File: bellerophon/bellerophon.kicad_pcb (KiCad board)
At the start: 2 copper layers, 55 x 98 mm, 27 parts, among them IC1 L7805ACV, IC2 Adafruit_MPL3115A2, Q1 IRLB8721PBF, Q2 IRLB8721PBF, U1 Adafruit_ICM20948, U2 Teensy4.0, U3 Adafruit SPI Flash SD Card

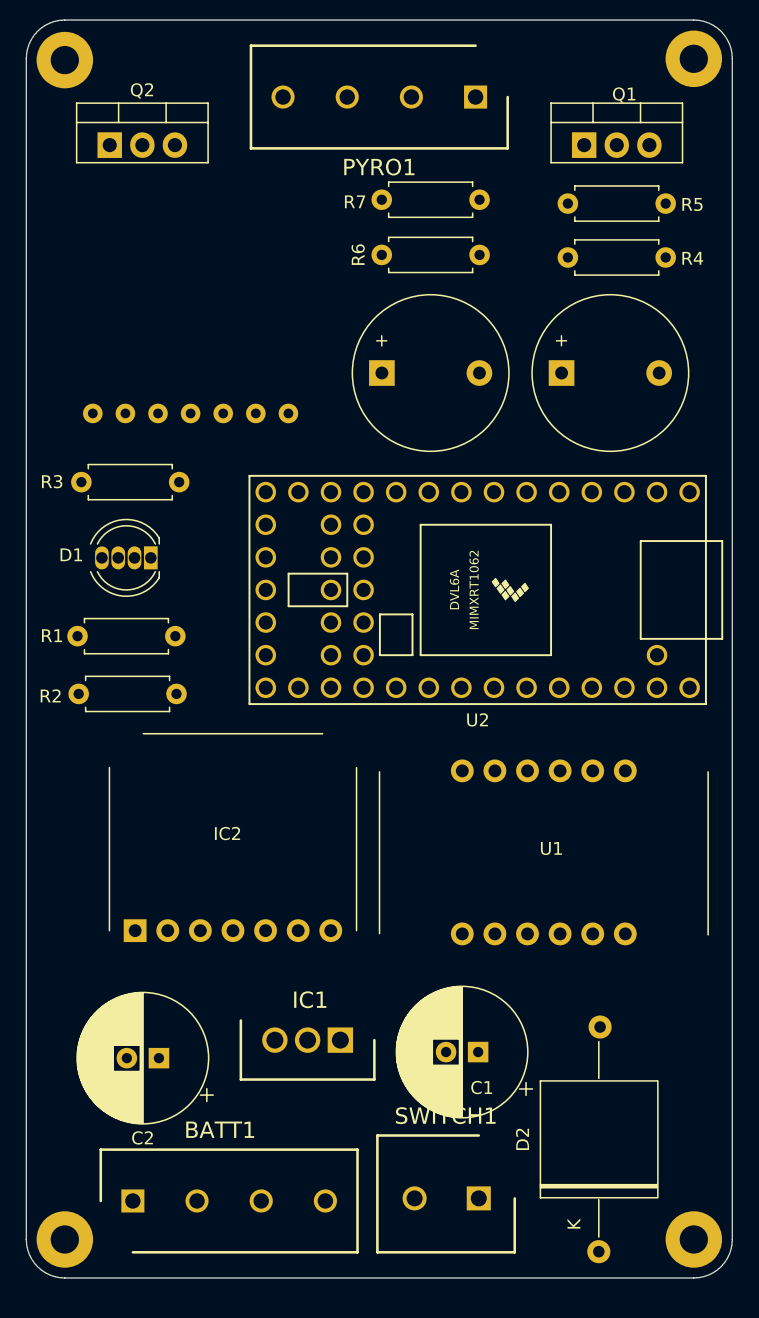
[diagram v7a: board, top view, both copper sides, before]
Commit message: refine silkscreen component description
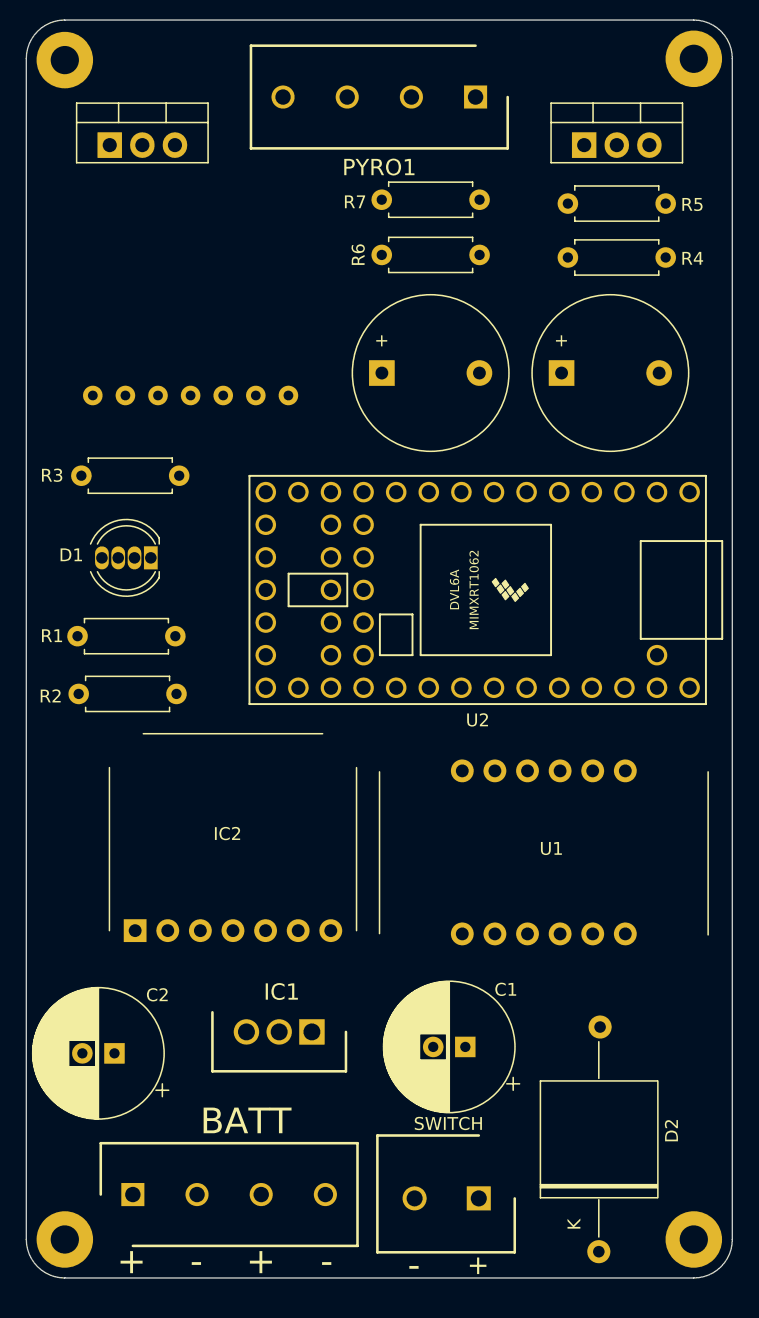
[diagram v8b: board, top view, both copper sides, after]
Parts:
- moved C2 3.49 mm to (66.9, 142.5)
- moved IC1 2.31 mm to (82.2, 140.8)
- moved U3 1.40 mm to (72.8, 84.9)
- moved C1 1.08 mm to (94.2, 142.0)
- moved BATT 0.50 mm to (68.3, 153.5)
- moved R3 0.50 mm to (71.9, 97.5)
- renumbered BATT1 to BATT, SWITCH1 to SWITCH
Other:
- board text added: "+"
- board text added: "-"
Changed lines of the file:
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@@
     (property "Sheetname" "")
     (attr through_hole)
-    (fp_text reference "Q1" (at 3.14 -3.945) (layer "F.SilkS")
-      (effects (font (size 1 1) (thickness 0.15)))
-    )
-    (fp_text value "IRLB8721PBF" (at 8.44 -0.9 90) (layer "F.Fab")
+    (fp_text reference "Q1" (at 9.04 -0.795) (layer "F.SilkS") hide
+      (effects (font (size 1 1) (thickness 0.15)))
+    )
+    (fp_text value "IRLB8721PBF" (at 2.69 -3.995 180) (layer "F.Fab")
       (effects (font (size 0.7 0.7) (thickness 0.1)))
     )
-    (fp_text user "${REFERENCE}" (at -4.26 -1.245) (layer "F.Fab")
+    (fp_text user "${REFERENCE}" (at 8.89 -1.095) (layer "F.Fab")
       (effects (font (size 1 1) (thickness 0.15)))
     )
@@
     (property "Sheetname" "")
     (attr through_hole)
-    (fp_text reference "D2" (at 0 -5.9 90 unlocked) (layer "F.SilkS")
-      (effects (font (size 1 1) (thickness 0.15)))
-    )
-    (fp_text value "DIODE" (at 1.4 6.3 90 unlocked) (layer "F.Fab")
+    (fp_text reference "D2" (at 0.675 5.7 90 unlocked) (layer "F.SilkS")
+      (effects (font (size 1 1) (thickness 0.15)))
+    )
+    (fp_text value "DIODE" (at 0.4 1.75 90 unlocked) (layer "F.Fab")
       (effects (font (size 1 1) (thickness 0.15)))
     )
@@
   )
   (footprint "Resistor_THT:R_Axial_DIN0207_L6.3mm_D2.5mm_P7.62mm_Horizontal" (layer "F.Cu")
-    (at 71.91 98 180)
+    (at 71.91 97.5 180)
     (descr "Resistor, Axial_DIN0207 series, Axial, Horizontal, pin pitch=7.62mm, 0.25W = 1/4W, length*diameter=6.3*2.5mm^2, http://cdn-reichelt.de/documents/datenblatt/B400/1_4W%23YAG.pdf")
     (tags "Resistor Axial_DIN0207 series Axial Horizontal pin pitch 7.62mm 0.25W = 1/4W length 6.3mm diameter 2.5mm")
@@
   )
   (footprint "RS-Components:TO255P460X1020X2008-3P" (layer "F.Cu")
-    (at 84.465 141.47 180)
+    (at 82.25 140.83 180)
     (descr "3-Pin TO-220")
     (tags "Integrated Circuit")
@@
   )
   (footprint "Adafruit:SD-CARD-B21.59x17.78mm-1X07_ROUND_70-P2.5mm" (layer "F.Cu")
-    (at 72.8 86.3)
+    (at 72.8 84.9)
     (property "Sheetfile" "bellerophon.kicad_sch")
     (property "Sheetname" "")
@@
   )
   (footprint "Capacitor_THT:CP_Radial_D10.0mm_P2.50mm" (layer "F.Cu")
-    (at 95.2 142.4 180)
+    (at 94.2 142 180)
     (descr "CP, Radial series, Radial, pin pitch=2.50mm, , diameter=10mm, Electrolytic Capacitor")
     (tags "CP Radial series Radial pin pitch 2.50mm  diameter 10mm Electrolytic Capacitor")
@@
     (property "Sheetname" "")
     (attr through_hole)
-    (fp_text reference "C1" (at -0.3 -2.8 180) (layer "F.SilkS")
-      (effects (font (size 1 1) (thickness 0.15)))
-    )
-    (fp_text value "0.33 uF" (at 1.25 6.25 180) (layer "F.Fab")
+    (fp_text reference "C1" (at -3.175 4.45 180) (layer "F.SilkS")
+      (effects (font (size 1 1) (thickness 0.15)))
+    )
+    (fp_text value "0.33 uF" (at 0.6 2.2) (layer "F.Fab")
       (effects (font (size 1 1) (thickness 0.15)))
     )
@@
     (property "Sheetname" "")
     (attr through_hole)
-    (fp_text reference "Q2" (at 2.54 -4.27) (layer "F.SilkS")
-      (effects (font (size 1 1) (thickness 0.15)))
-    )
-    (fp_text value "IRLB8721PBF" (at 8.44 -0.945 90) (layer "F.Fab")
+    (fp_text reference "Q2" (at 9 -0.795) (layer "F.SilkS") hide
+      (effects (font (size 1 1) (thickness 0.15)))
+    )
+    (fp_text value "IRLB8721PBF" (at 2.9 -4.145 180) (layer "F.Fab")
       (effects (font (size 0.7 0.7) (thickness 0.1)))
     )
-    (fp_text user "${REFERENCE}" (at 2.54 -4.27) (layer "F.Fab")
+    (fp_text user "${REFERENCE}" (at 9.15 -0.945) (layer "F.Fab")
       (effects (font (size 1 1) (thickness 0.15)))
     )
@@
       (effects (font (size 1 1) (thickness 0.15)))
     )
-    (fp_text value "Buzzer" (at 3.8 7.4) (layer "F.Fab")
+    (fp_text value "Buzzer" (at 3.75 3.05) (layer "F.Fab")
       (effects (font (size 1 1) (thickness 0.15)))
     )
@@
       (effects (font (size 1 1) (thickness 0.15)))
     )
-    (fp_text value "Buzzer" (at 3.8 7.4) (layer "F.Fab")
+    (fp_text value "Buzzer" (at 3.8 3.25) (layer "F.Fab")
       (effects (font (size 1 1) (thickness 0.15)))
     )
@@
   )
   (footprint "RS-Components:SHDR4W100P0X500_1X4_2000X800X1000P" (layer "F.Cu")
-    (at 68.3 154)
+    (at 68.3 153.5)
     (descr "REFP1/AIN6")
     (tags "Connector")
@@
     (property "Sheetname" "")
     (attr through_hole)
-    (fp_text reference "BATT1" (at 6.8 -5.5) (layer "F.SilkS")
-      (effects (font (size 1.27 1.27) (thickness 0.254)))
+    (fp_text reference "BATT" (at 8.8 -5.7) (layer "F.SilkS")
+      (effects (font (size 2 2) (thickness 0.3)))
     )
     (fp_text value "Screw_Terminal_01x04" (at 0 0) (layer "F.SilkS") hide
       (effects (font (size 1.27 1.27) (thickness 0.254)))
     )
-    (fp_text user "${REFERENCE}" (at 6.8 -5.5) (layer "F.Fab")
+    (fp_text user "${REFERENCE}" (at 8.525 -2.275) (layer "F.Fab")
       (effects (font (size 1.27 1.27) (thickness 0.254)))
     )
@@
     (property "Sheetname" "")
     (attr through_hole)
-    (fp_text reference "SWITCH1" (at 2.55 6.4) (layer "F.SilkS")
-      (effects (font (size 1.27 1.27) (thickness 0.254)))
+    (fp_text reference "SWITCH" (at 2.35 5.8) (layer "F.SilkS")
+      (effects (font (size 1 1) (thickness 0.2)))
     )
     (fp_text value "Screw_Terminal_01x04" (at 0 0) (layer "F.SilkS") hide
       (effects (font (size 1.27 1.27) (thickness 0.254)))
     )
-    (fp_text user "${REFERENCE}" (at 2.55 6.4) (layer "F.Fab")
+    (fp_text user "${REFERENCE}" (at 2.4 2.6) (layer "F.Fab")
       (effects (font (size 1.27 1.27) (thickness 0.254)))
     )
@@
       (effects (font (size 1 1) (thickness 0.15)))
     )
-    (fp_text value "Teensy4.0" (at -0.135 4.1) (layer "F.Fab")
+    (fp_text value "Teensy4.0" (at -7.585 -0.5 90) (layer "F.Fab")
       (effects (font (size 1 1) (thickness 0.15)))
     )
@@
   )
   (footprint "Capacitor_THT:CP_Radial_D10.0mm_P2.50mm" (layer "F.Cu")
-    (at 70.332677 142.875 180)
+    (at 66.867677 142.5 180)
     (descr "CP, Radial series, Radial, pin pitch=2.50mm, , diameter=10mm, Electrolytic Capacitor")
     (tags "CP Radial series Radial pin pitch 2.50mm  diameter 10mm Electrolytic Capacitor")
@@
     (property "Sheetname" "")
     (attr through_hole)
-    (fp_text reference "C2" (at 1.25 -6.25 180) (layer "F.SilkS")
+    (fp_text reference "C2" (at -3.367323 4.525 180) (layer "F.SilkS")
       (effects (font (size 1 1) (thickness 0.15)))
     )
@@
   (gr_line (start 115 157) (end 115 65) (layer "Edge.Cuts") (width 0.1))
   (gr_arc (start 112 62) (mid 114.12132 62.87868) (end 115 65) (layer "Edge.Cuts") (width 0.1))
+  (gr_text "+" (at 68.2 158.7) (layer "F.SilkS")
+    (effects (font (size 2 2) (thickness 0.3)))
+  )
+  (gr_text "-" (at 90.2 159) (layer "F.SilkS")
+    (effects (font (size 2 2) (thickness 0.3)))
+  )
+  (gr_text "-" (at 73.25 158.7) (layer "F.SilkS")
+    (effects (font (size 2 2) (thickness 0.3)))
+  )
+  (gr_text "+" (at 78.275 158.7) (layer "F.SilkS")
+    (effects (font (size 2 2) (thickness 0.3)))
+  )
+  (gr_text "-" (at 83.4 158.7) (layer "F.SilkS")
+    (effects (font (size 2 2) (thickness 0.3)))
+  )
+  (gr_text "+" (at 95.2 159) (layer "F.SilkS")
+    (effects (font (size 1.5 1.5) (thickness 0.3)))
+  )
 )
